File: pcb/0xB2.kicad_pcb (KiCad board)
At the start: 2 copper layers, 41.8 x 50.8 mm, 58 parts, among them J1 USB_C_Receptacle_USB2.0, J10 RGB, J11 serial, J5 Conn_01x02, J6 Ribbon, J7 Ribbon, J8 trackball, J9 Serial, SW2 SW_Push, SW3 SW_SPST, U1 RP2040, U2 GD25Q80CEIGR, U3 XC6210B332MR-G, Y1 Crystal_GND24

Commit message: daughterboard work
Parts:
- added J12: Conn_01x02_Female, Library:PinHeader_1x02_P2.54mm_Vertical, F.Cu at (185.1, 86.8)
- added J13: Conn_01x02_Female, Library:PinHeader_1x02_P2.54mm_Vertical, F.Cu at (202.3, 86.9)
- added J14: Conn_01x02_Female, Library:PinHeader_1x02_P2.54mm_Vertical, F.Cu at (144.7, 84.2)
- added J15: Conn_01x02_Female, Library:PinHeader_1x02_P2.54mm_Vertical, F.Cu at (161.9, 81.8)
- added kibuzzard-61F01B61: G***, kibuzzard-61F01B61, F.Cu at (192.3, 84.0)
- added kibuzzard-61F01B61: G***, kibuzzard-61F01B61, B.Cu at (192.2, 84.1)
- added kibuzzard-6284F97C: G***, kibuzzard-6284F97C, F.Cu at (193.5, 92.4)
- moved R5 42.1 mm to (190.3, 91.0), turned to 180 degrees
- moved J1 40.7 mm to (192.8, 87.4)
- moved FB1 40.2 mm to (187.2, 90.5)
- moved R4 37.1 mm to (194.6, 91.0), turned to 0 degrees
- moved R14 10.8 mm to (175.3, 74.0)
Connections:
- J1 pad A4: VBUS -> Net-(J1-PadA4)
- J1 pad A6: /D+ -> Net-(J1-PadA6)
- J1 pad A7: /D- -> Net-(J1-PadA7)
- J1 pad A9: VBUS -> Net-(J1-PadA4)
- J1 pad B4: VBUS -> Net-(J1-PadA4)
- J1 pad B6: /D+ -> Net-(J1-PadA6)
- J1 pad B7: /D- -> Net-(J1-PadA7)
- J1 pad B9: VBUS -> Net-(J1-PadA4)
- SW3 pad 1: /~{RESET} -> GND
- SW3 pad 2: GND -> /~{RESET}
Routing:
- net Net-(J1-PadA7): track 0.00 -> 17.6 mm
- net Net-(J1-PadA6): track 0.00 -> 16.7 mm
- net +5V: track 55.5 -> 63.7 mm
- net /D-: track 10.2 -> 17.0 mm, vias 2 -> 1
- net /D+: track 9.12 -> 15.5 mm, vias 2 -> 1
- net Net-(J1-PadA4): track 0.00 -> 5.15 mm, vias 0 -> 2
- net Net-(J1-PadB5): track 6.15 -> 2.23 mm
- net /~{RESET}: track 26.4 -> 29.9 mm
- net Net-(J1-PadA5): track 5.60 -> 2.21 mm
- net GND: track 44.6 -> 42.0 mm, vias 28 -> 31
- net VBUS: track 19.5 -> 17.2 mm, vias 4 -> 2
- net /D6: track 32.4 -> 33.2 mm
- net /D5: track 30.4 -> 31.2 mm
- net /D4: track 27.7 -> 28.5 mm
- net /D9: track 37.4 -> 38.1 mm
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- removed copper zone on F.Cu, net GND
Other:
- board size 41.8 x 50.8 mm -> 70.9 x 50.8 mm
- board text added: "D+"
- board text added: "D-"
- board text added: "Solder on this side"
- board text added: "VBUS"

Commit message: cleanup
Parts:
- removed FB1: FerriteBead_Small, Inductor_SMD:L_0603_1608Metric
- removed J1: USB_C_Receptacle_USB2.0, 0xLib_USB_Type-C:USB_C_Receptacle_HRO_TYPE-C-31-M-14
- removed J12, J13: Conn_01x02_Female, Library:PinHeader_1x02_P2.54mm_Vertical
- removed R4, R5: 5.1k, Resistor_SMD:R_0402_1005Metric
- removed kibuzzard-61F01B61 (x2): G***, kibuzzard-61F01B61
- removed kibuzzard-6284F97C: G***, kibuzzard-6284F97C
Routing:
- net Net-(FB1-Pad2): track 23.9 -> 0.00 mm
- net Net-(J1-PadA7): track 17.6 -> 0.00 mm
- net Net-(J1-PadA6): track 16.7 -> 0.00 mm
- net Net-(J1-PadA4): track 5.15 -> 0.00 mm, vias 2 -> 0
- net GND: track 42.0 -> 37.8 mm, vias 31 -> 26
- net Net-(J1-PadB5): track 2.23 -> 0.00 mm
- net Net-(J1-PadA5): track 2.21 -> 0.00 mm
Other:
- board size 70.9 x 50.8 mm -> 41.8 x 50.8 mm
- board text removed: "Solder on this side"

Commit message: silkscreen
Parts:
- added kibuzzard-61F01C84: G***, kibuzzard-61F01C84, F.Cu at (163.9, 95.2)
- added kibuzzard-61F01C84: G***, kibuzzard-61F01C84, B.Cu at (163.9, 95.2)

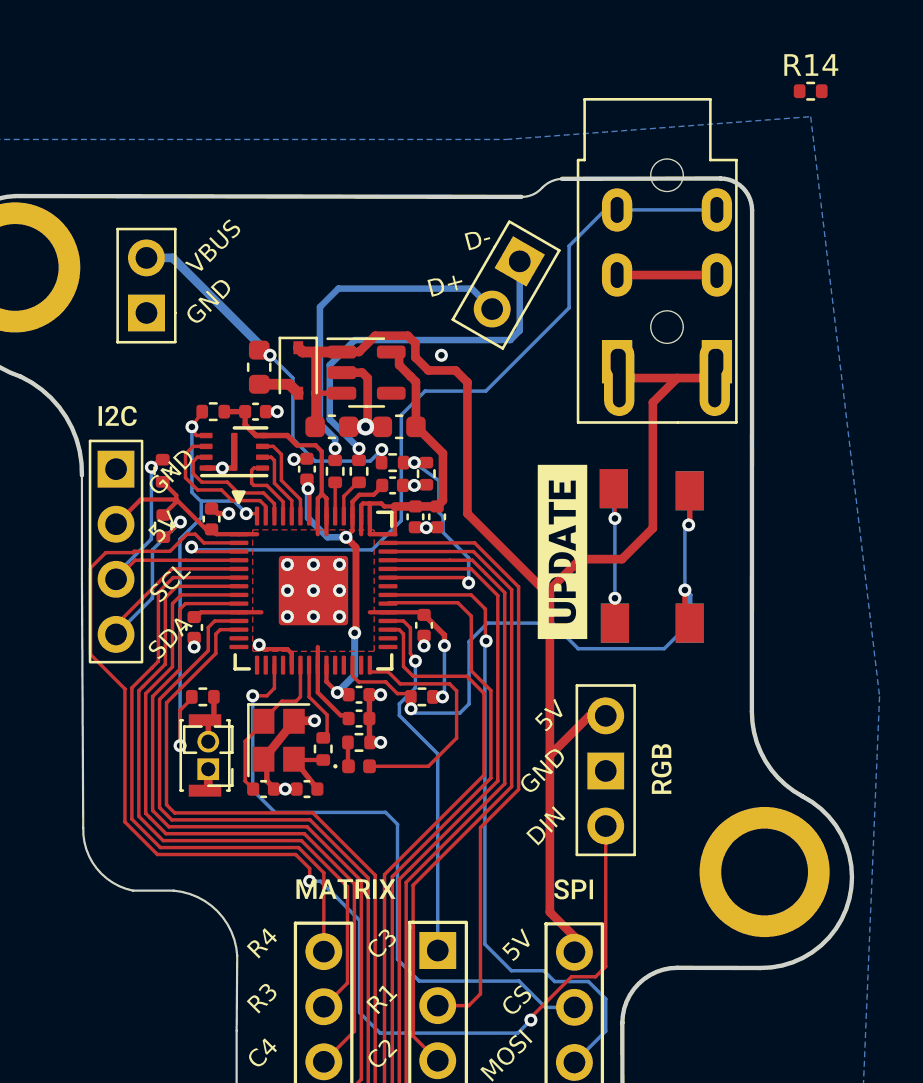
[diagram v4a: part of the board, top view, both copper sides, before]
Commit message: move daughterboard to its own repo
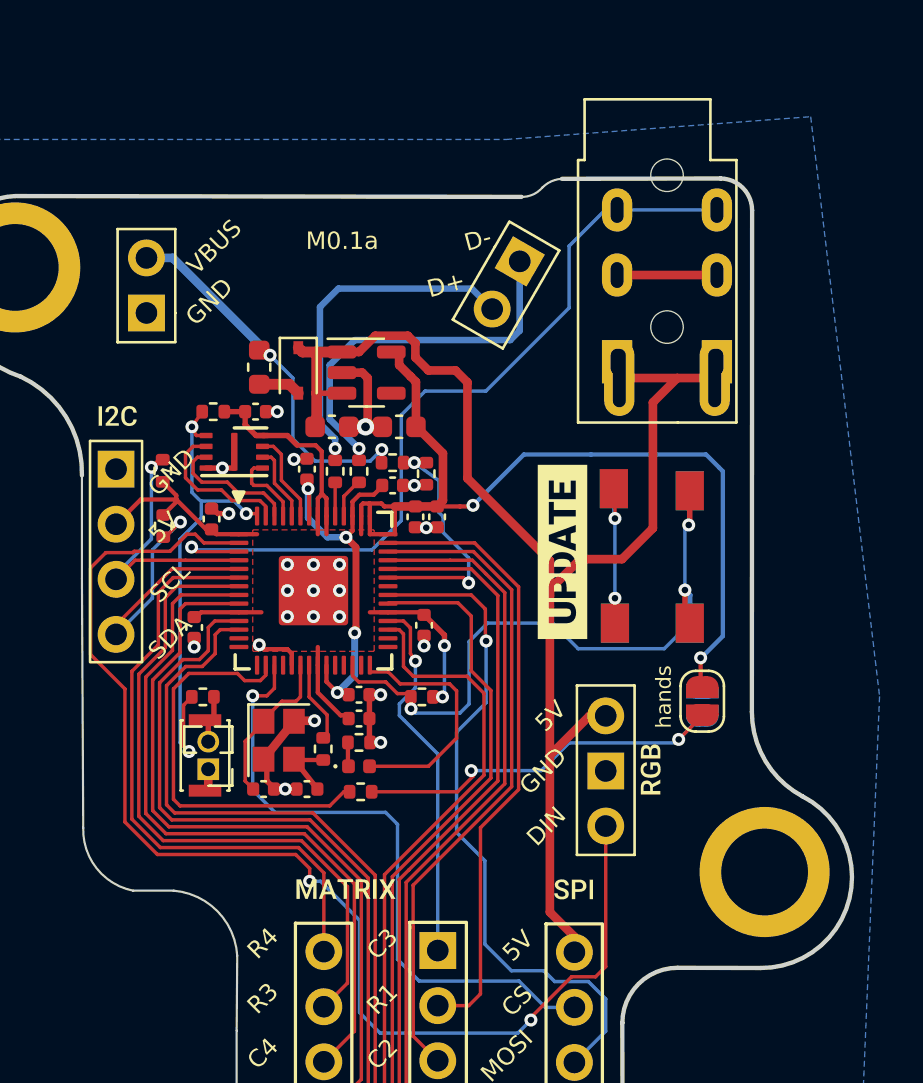
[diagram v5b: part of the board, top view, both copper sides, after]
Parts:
- added JP1: Jumper_2_Open, Library:SolderJumper-2_P1.3mm_Open_RoundedPad1.0x1.5mm, F.Cu at (170.3, 102.1)
- added JP2: Jumper_2_Open, Library:SolderJumper-2_P1.3mm_Open_RoundedPad1.0x1.5mm, B.Cu at (170.3, 102.1)
- moved R14 38.4 mm to (154.6, 106.3)
- moved kibuzzard-61F019CB 0.51 mm to (167.9, 105.2)
- moved kibuzzard-61F019CB 0.51 mm to (167.9, 105.3)
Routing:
- net +3V3: track 52.7 -> 77.3 mm, vias 2 -> 4
- net /D13: track 0.00 -> 18.9 mm
- net Net-(JP1-Pad1): track 0.00 -> 18.5 mm, vias 0 -> 2
- net /~{RESET}: track 29.9 -> 31.5 mm
- net /MOSI: track 30.4 -> 31.5 mm
- net /QSPI_~{CS}: track 22.4 -> 23.1 mm
- net GND: vias 26 -> 25
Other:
- board text added: "M0.1a"
- board text added: "hands"

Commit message: silkscreen
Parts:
- removed rb_cake: G*****, 0xB2_drawings:rb_cake
- removed splinky: G*****, 0xB2_drawings:splinky
- added G***: LOGO, LOGO, B.Cu at (154.5, 96.2)
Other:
- board text added: "0.1a"
- board text removed: "0xB2"
- board text removed: "v2"

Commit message: version
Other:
- board text removed: "M0.1a"
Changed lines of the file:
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@@
     (effects (font (size 0.8 0.8) (thickness 0.15)) (justify mirror))
-  )
-  (gr_text "0.1a" (at 144.75 86.6) (layer "B.SilkS")
-    (effects (font (size 0.6 0.6) (thickness 0.15)) (justify mirror))
   )
   (gr_text "5V" (at 162.880222 102.72 -45) (layer "B.SilkS")
@@
     (effects (font (size 0.8 0.8) (thickness 0.15)) (justify mirror))
   )
-  (gr_text "M0.1a" (at 153.775 80.875) (layer "B.SilkS")
+  (gr_text "0.1a" (at 153.775 80.875) (layer "B.SilkS")
     (effects (font (size 0.8 0.8) (thickness 0.15)) (justify mirror))
   )
@@
     (effects (font (size 0.8 0.8) (thickness 0.15)))
   )
-  (gr_text "0.1a" (at 144.85 86.7) (layer "F.SilkS")
-    (effects (font (size 0.6 0.6) (thickness 0.15)))
-  )
   (gr_text "C5" (at 150.064724 120.880001 45) (layer "F.SilkS")
     (effects (font (size 0.8 0.8) (thickness 0.15)))
@@
     (effects (font (size 0.8 0.8) (thickness 0.15)))
   )
-  (gr_text "M0.1a" (at 153.725 80.875) (layer "F.SilkS")
+  (gr_text "0.1a" (at 153.725 80.875) (layer "F.SilkS")
     (effects (font (size 0.8 0.8) (thickness 0.15)))
   )

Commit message: silkscreen
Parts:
- moved kibuzzard-61F01940 0.47 mm to (153.9, 111.2) (x2)
- moved kibuzzard-61F01957 0.47 mm to (164.4, 111.2) (x2)
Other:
- board text added: "0.1b"
- board text added: "rp2040 shield"
- board text removed: "0.1a"
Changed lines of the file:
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@@
   )
   (footprint "kibuzzard-61F01957" (layer "F.Cu")
-    (at 164.393416 110.775)
+    (at 164.363416 111.248074)
     (descr "Converted using: scripting")
     (tags "svg2mod")
@@
   )
   (footprint "kibuzzard-61F01940" (layer "F.Cu")
-    (at 153.9 110.762597)
+    (at 153.87 111.235671)
     (descr "Converted using: scripting")
     (tags "svg2mod")
@@
   )
   (footprint "kibuzzard-61F01957" (layer "B.Cu")
-    (at 164.473416 110.775 180)
+    (at 164.443416 111.248074 180)
     (descr "Converted using: scripting")
     (tags "svg2mod")
@@
   )
   (footprint "kibuzzard-61F01940" (layer "B.Cu")
-    (at 153.95 110.762597 180)
+    (at 153.92 111.235671 180)
     (descr "Converted using: scripting")
     (tags "svg2mod")
@@
     (effects (font (size 0.8 0.8) (thickness 0.15)) (justify mirror))
   )
-  (gr_text "0.1a" (at 153.775 80.875) (layer "B.SilkS")
-    (effects (font (size 0.8 0.8) (thickness 0.15)) (justify mirror))
-  )
   (gr_text "D+" (at 158.262792 82.750694 -15) (layer "B.SilkS")
     (effects (font (size 0.8 0.8) (thickness 0.15)) (justify mirror))
@@
     (effects (font (size 0.8 0.8) (thickness 0.15)) (justify mirror))
   )
+  (gr_text "rp2040 shield" (at 147.74 108.43) (layer "B.SilkS")
+    (effects (font (size 0.8 0.8) (thickness 0.12)) (justify mirror))
+  )
   (gr_text "C6" (at 149.988524 123.420001 315) (layer "B.SilkS")
     (effects (font (size 0.8 0.8) (thickness 0.15)) (justify mirror))
@@
     (effects (font (size 0.8 0.8) (thickness 0.15)))
   )
+  (gr_text "rp2040 shield" (at 147.74 108.4) (layer "F.SilkS")
+    (effects (font (size 0.8 0.8) (thickness 0.12)))
+  )
   (gr_text "R5" (at 150.090124 125.954059 45) (layer "F.SilkS")
     (effects (font (size 0.8 0.8) (thickness 0.15)))
@@
     (effects (font (size 0.8 0.8) (thickness 0.15)))
   )
-  (gr_text "0.1a" (at 153.725 80.875) (layer "F.SilkS")
+  (gr_text "0.1b" (at 167.925 113.25) (layer "F.SilkS")
     (effects (font (size 0.8 0.8) (thickness 0.15)))
   )
